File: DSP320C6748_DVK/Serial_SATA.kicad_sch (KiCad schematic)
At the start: 10 parts, among them IC6 CP2102C-A01-GQFN24, J3 USB_Type_C

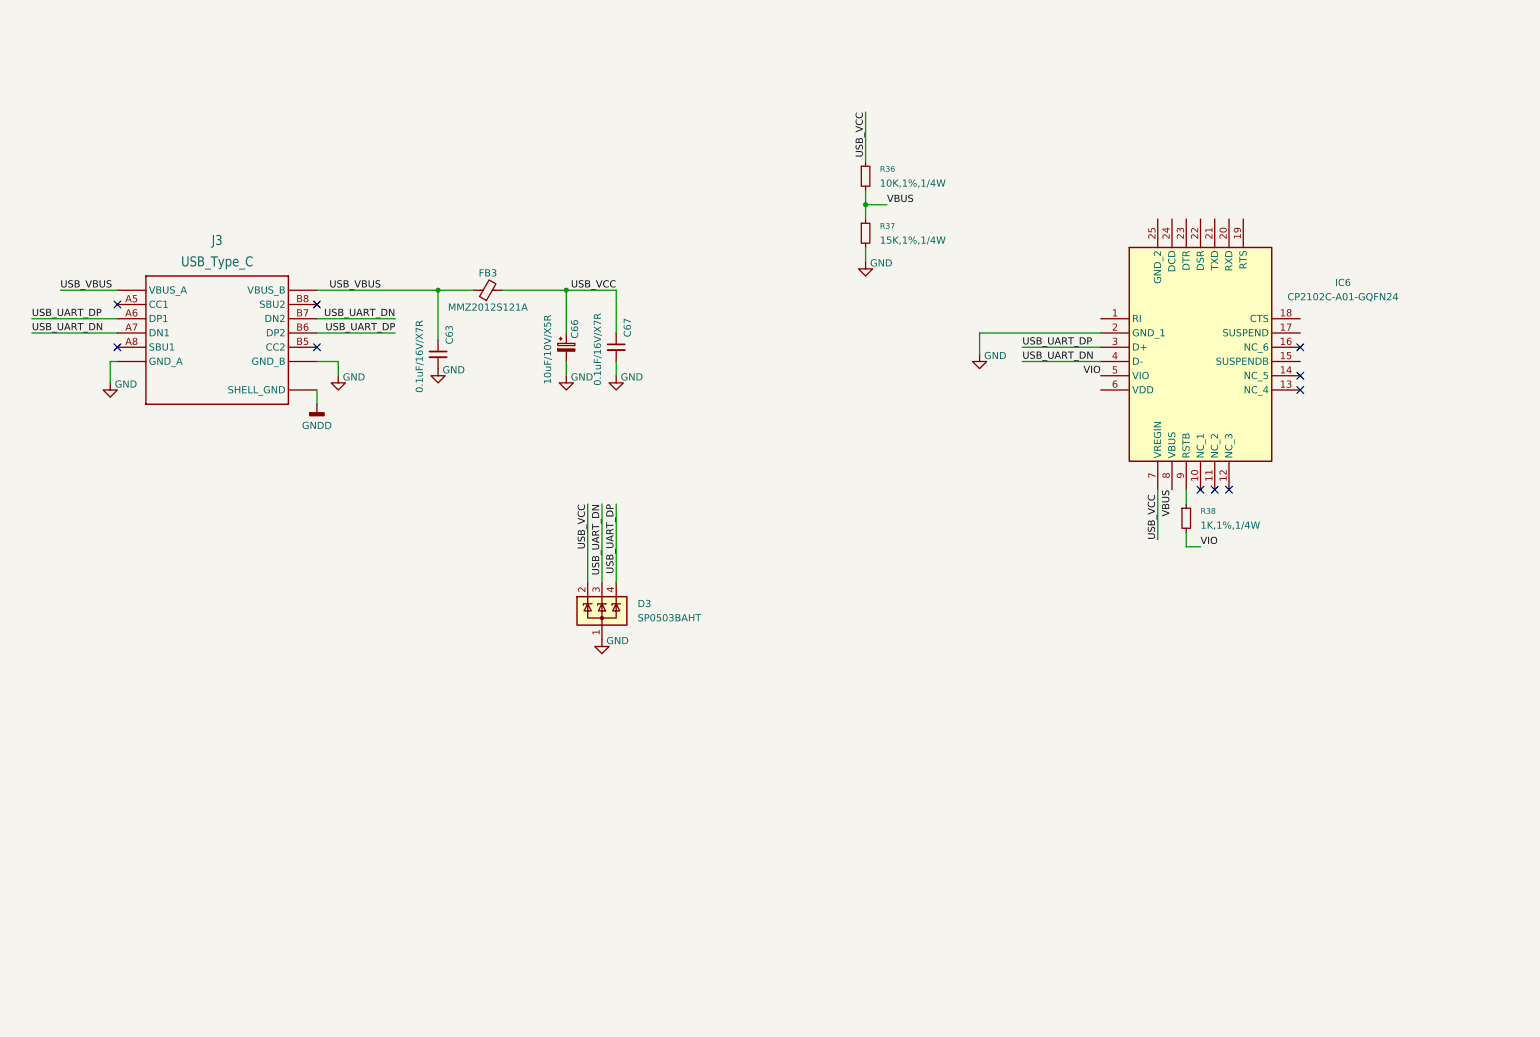
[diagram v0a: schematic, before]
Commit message: Serial Circuit completed, SATA section Added, DSP Reset Section Added
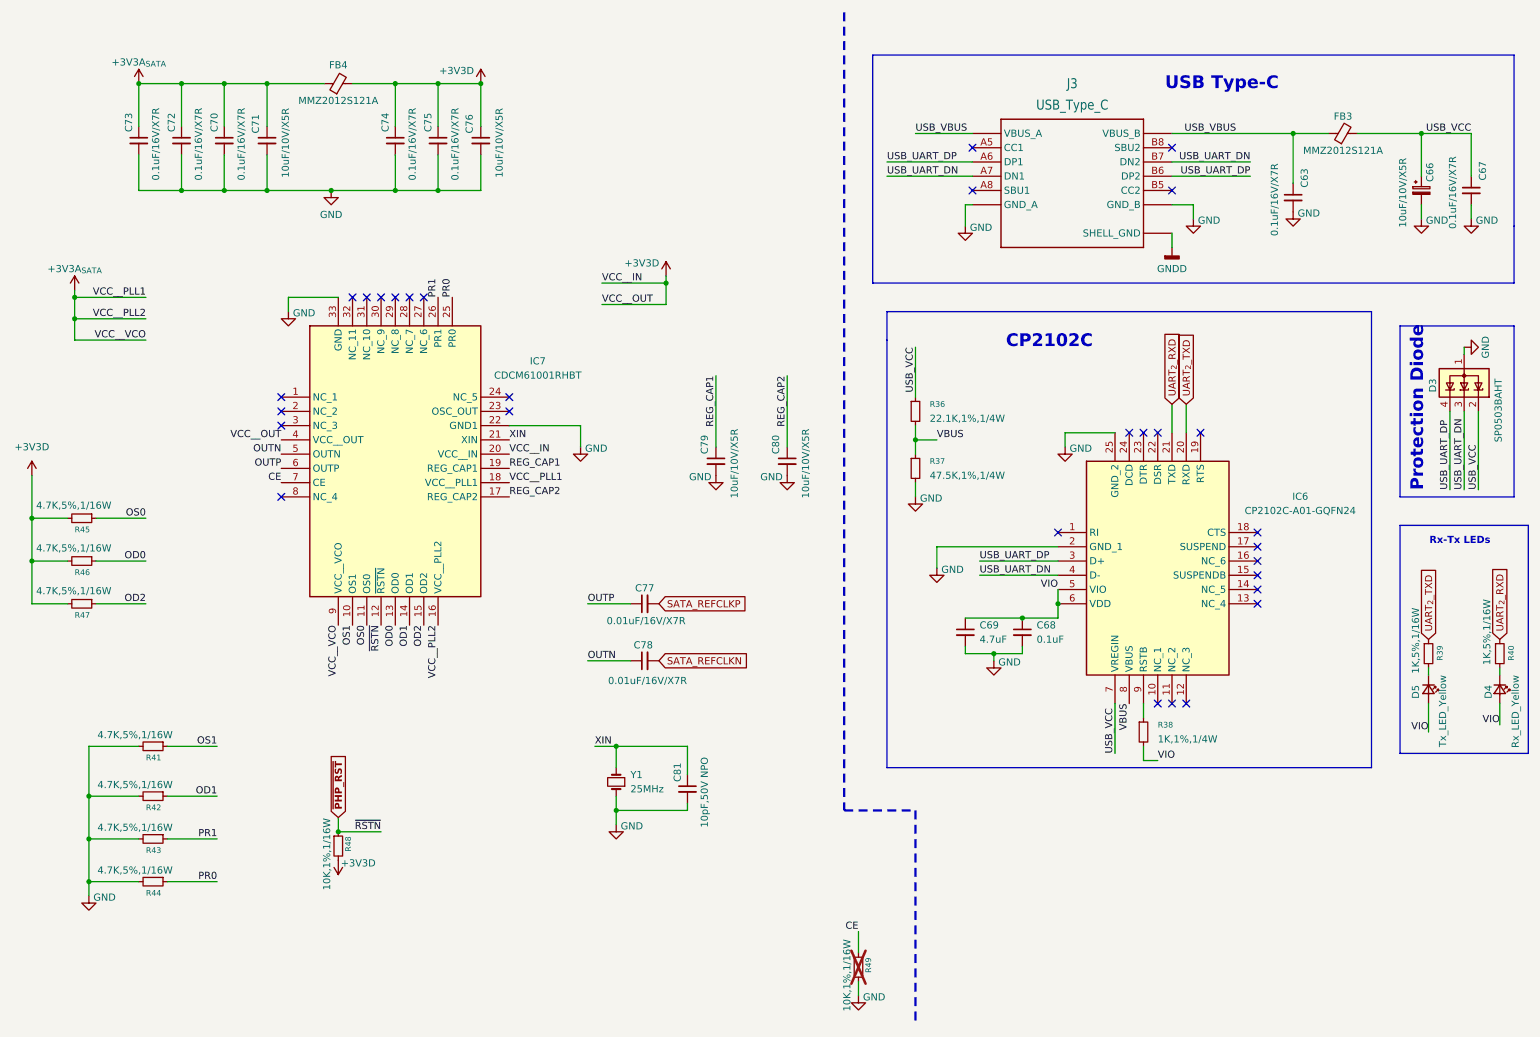
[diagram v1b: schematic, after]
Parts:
- added C68: 0.1uF, symbol Device:C_Small
- added C69: 4.7uF, symbol Device:C_Small
- added C70, C72, C73, C74, C75: 0.1uF/16V/X7R, symbol Device:C_Small
- added C71, C76, C79, C80: 10uF/10V/X5R, symbol Device:C_Small
- added C77, C78: 0.01uF/16V/X7R, symbol Device:C_Small
- added C81: 10pF,50V NPO, symbol Device:C_Small
- added D4: Rx_LED_Yellow, symbol Device:LED_Small
- added D5: Tx_LED_Yellow, symbol Device:LED_Small
- added FB4: MMZ2012S121A, symbol Device:FerriteBead_Small
- added IC7: CDCM61001RHBT, QFN50P500X500X100-33N-D, symbol CDCM61001RHBT:CDCM61001RHBT
- added R39, R40: 1K,5%,1/16W, symbol Device:R_Small
- added R41, R42, R43, R44, R45, R46, R47: 4.7K,5%,1/16W, symbol Device:R_Small
- added R48, R49: 10K,1%,1/16W, symbol Device:R_Small
- added Y1: 25MHz, symbol Device:Crystal_Small
- R36: value 10K,1%,1/4W -> 22.1K,1%,1/4W
- R37: value 15K,1%,1/4W -> 47.5K,1%,1/4W
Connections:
- net GND: now also IC6.25 (GND_2), C68.2, C69.2, C70.2, C71.2, C72.2, C73.2, C74.2, C75.2, C76.2, C79.2, C80.2, C81.2, IC7.22 (GND1), IC7.33 (GND), R41.2, R42.2, R43.2, R44.2, R49.2, Y1.1
- net VIO: now also IC6.6 (VDD), C68.1, C69.1, D4.2 (A), D5.2 (A)
- net UART_{2}_TXD: now reaches IC6.20 (RXD)
- net UART_{2}_TXD: now also R39.1
- net UART_{2}_RXD: now reaches IC6.21 (TXD)
- net UART_{2}_RXD: now also R40.1
- new net: D5.1 (K), R39.2
- new net: D4.1 (K), R40.2
- new net +3V3A_{SATA}: C70.1, C71.1, C72.1, C73.1, FB4.1, IC7.16 (VCC__PLL2), IC7.18 (VCC__PLL1), IC7.9 (VCC__VCO)
- new net +3V3D: C74.1, C75.1, C76.1, FB4.2, IC7.20 (VCC__IN), IC7.4 (VCC__OUT), R45.2, R46.2, R47.2, R48.2
- new net CE: IC7.7 (CE), R49.1
- new net OD0: IC7.13 (OD0), R46.1
- new net OD1: IC7.14 (OD1), R42.1
- new net OD2: IC7.15 (OD2), R47.1
- new net OS0: IC7.11 (OS0), R45.1
- new net OS1: IC7.10 (OS1), R41.1
- new net OUTN: C78.1, IC7.5 (OUTN)
- new net OUTP: C77.1, IC7.6 (OUTP)
- new net PR0: IC7.25 (PR0), R44.1
- new net PR1: IC7.26 (PR1), R43.1
- new net REG_CAP1: C79.1, IC7.19 (REG_CAP1)
- new net REG_CAP2: C80.1, IC7.17 (REG_CAP2)
- new net SATA_REFCLKN: C78.2
- new net SATA_REFCLKP: C77.2
- new net XIN: C81.1, IC7.21 (XIN), Y1.2
- new net ~{PHP_RST}: IC7.12 (~{RSTN}), R48.1
- no-connect marks 10 -> 30
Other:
- note added: "CP2102C"
- note added: "Protection Diode"
- note added: "Rx-Tx LEDs"
- note added: "USB Type-C"
- moved on the sheet: C63, C66, C67, D3, FB3, IC6, J3, R36, R37, R38

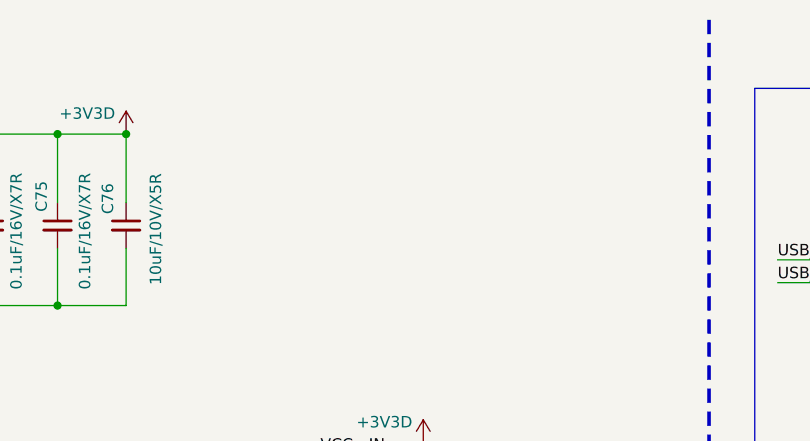
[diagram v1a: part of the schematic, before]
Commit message: Partial VGA-LCD schematic added
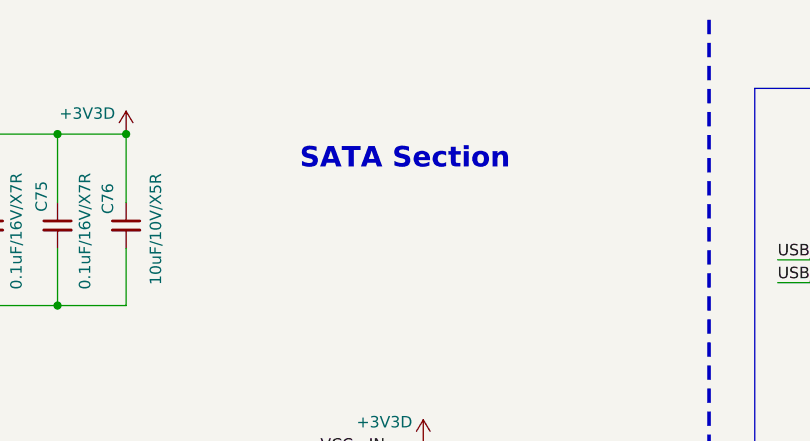
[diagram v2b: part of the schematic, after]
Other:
- note added: "SATA Section"
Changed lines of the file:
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@@
+		)
+	)
+	(text "SATA Section"
+		(exclude_from_sim no)
+		(at 126.238 30.734 0)
+		(effects
+			(font
+				(size 2.27 2.27)
+				(thickness 0.454)
+				(bold yes)
+			)
 		)
 	)

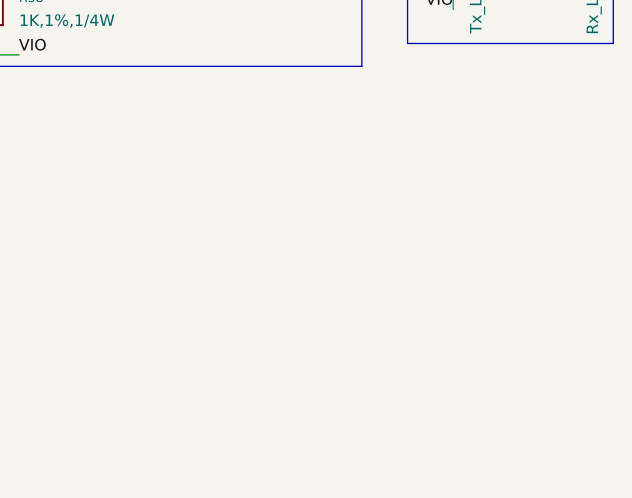
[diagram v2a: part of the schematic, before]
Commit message: DDR_RAM and Video Decoder Schematic Added
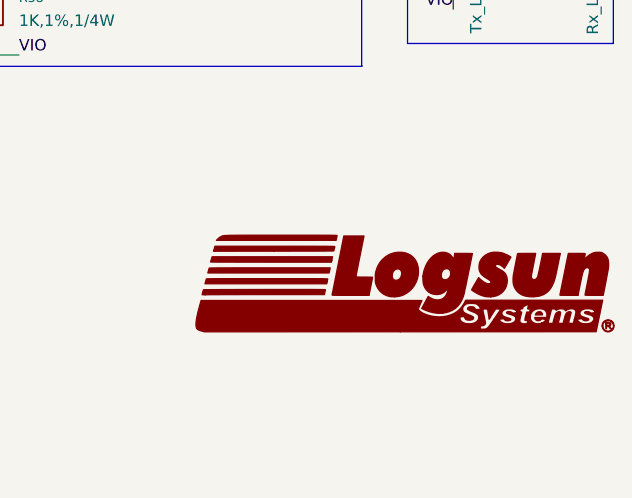
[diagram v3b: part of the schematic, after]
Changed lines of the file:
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@@
+	)
+	(symbol
+		(lib_id "Logsun_Logo:LOGO")
+		(at 259.08 173.99 0)
+		(unit 1)
+		(body_style 1)
+		(exclude_from_sim no)
+		(in_bom yes)
+		(on_board yes)
+		(in_pos_files yes)
+		(dnp no)
+		(fields_autoplaced yes)
+		(property "Reference" "#G7"
+			(at 259.08 168.025 0)
+			(hide yes)
+			(show_name no)
+			(do_not_autoplace no)
+			(effects
+				(font
+					(size 1.27 1.27)
+				)
+			)
+		)
+		(property "Value" "LOGO"
+			(at 259.08 179.955 0)
+			(hide yes)
+			(show_name no)
+			(do_not_autoplace no)
+			(effects
+				(font
+					(size 1.27 1.27)
+				)
+			)
+		)
+		(property "Footprint" ""
+			(at 259.08 173.99 0)
+			(hide yes)
+			(show_name no)
+			(do_not_autoplace no)
+			(effects
+				(font
+					(size 1.27 1.27)
+				)
+			)
+		)
+		(property "Datasheet" ""
+			(at 259.08 173.99 0)
+			(hide yes)
+			(show_name no)
+			(do_not_autoplace no)
+			(effects
+				(font
+					(size 1.27 1.27)
+				)
+			)
+		)
+		(property "Description" ""
+			(at 259.08 173.99 0)
+			(hide yes)
+			(show_name no)
+			(do_not_autoplace no)
+			(effects
+				(font
+					(size 1.27 1.27)
+				)
+			)
+		)
+		(instances
+			(project "DSP320C6748_DVK"
+				(path "/3a70ffc0-9fe7-4a5b-b3c2-23140355df82/1c65a424-dd23-4a5f-aa20-bdb9d16cf58b"
+					(reference "#G7")
+					(unit 1)
+				)
+			)
+		)
 	)
 	(symbol

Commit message: Whole Schematic Reannotation Done
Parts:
- renumbered C73 to C72, C72 to C73, C70 to C74, C71 to C75, C74 to C76, C75 to C77, C76 to C78, C77 to C79, C78 to C80, C79 to C82, C80 to C83, C69 to C84, C68 to C85, C63 to C86, C66 to C87, C67 to C88, D3 to D6, D4 to D7, FB4 to FB3, FB3 to FB4, IC6 to IC10, IC7 to IC9, J3 to J5, R45 to R72, R46 to R73, R47 to R74, R41 to R75, R42 to R76, R43 to R77, R44 to R78, R48 to R79, R49 to R80, R36 to R81, R37 to R82, R38 to R83, R39 to R84, R40 to R85, Y1 to Y3

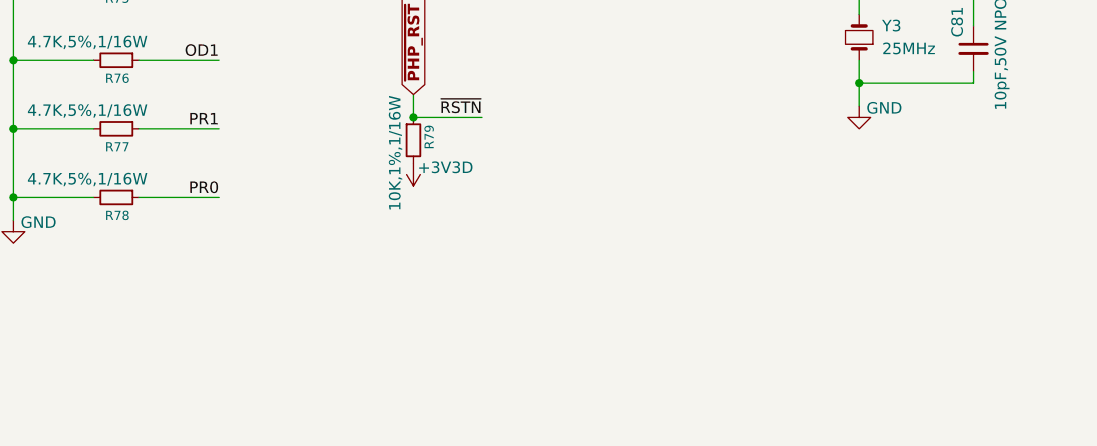
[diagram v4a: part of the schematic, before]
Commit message: SATA Connector Added
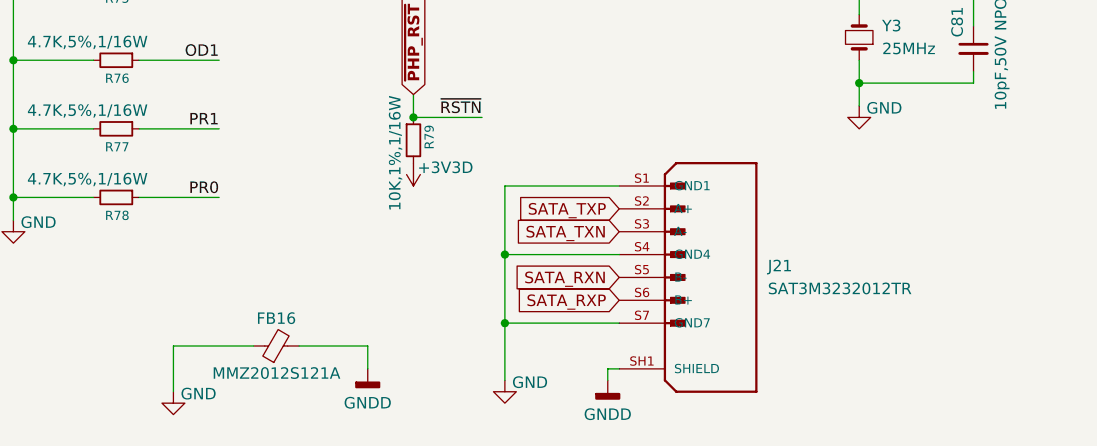
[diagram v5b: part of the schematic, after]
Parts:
- added FB16: MMZ2012S121A, symbol Device:FerriteBead_Small
- added J21: SAT3M3232012TR, SAT3M3232012TR:AMPHENOL_SAT3M3232012TR, symbol SAT3M3232012TR:SAT3M3232012TR
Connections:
- net GND: now also FB16.1, J21.S1 (GND1), J21.S4 (GND4), J21.S7 (GND7)
- net GNDD: now also FB16.2, J21.SH1 (SHIELD), J21.SH2 (SHIELD)
- new net SATA_RXN: J21.S5 (B-)
- new net SATA_RXP: J21.S6 (B+)
- new net SATA_TXN: J21.S3 (A-)
- new net SATA_TXP: J21.S2 (A+)

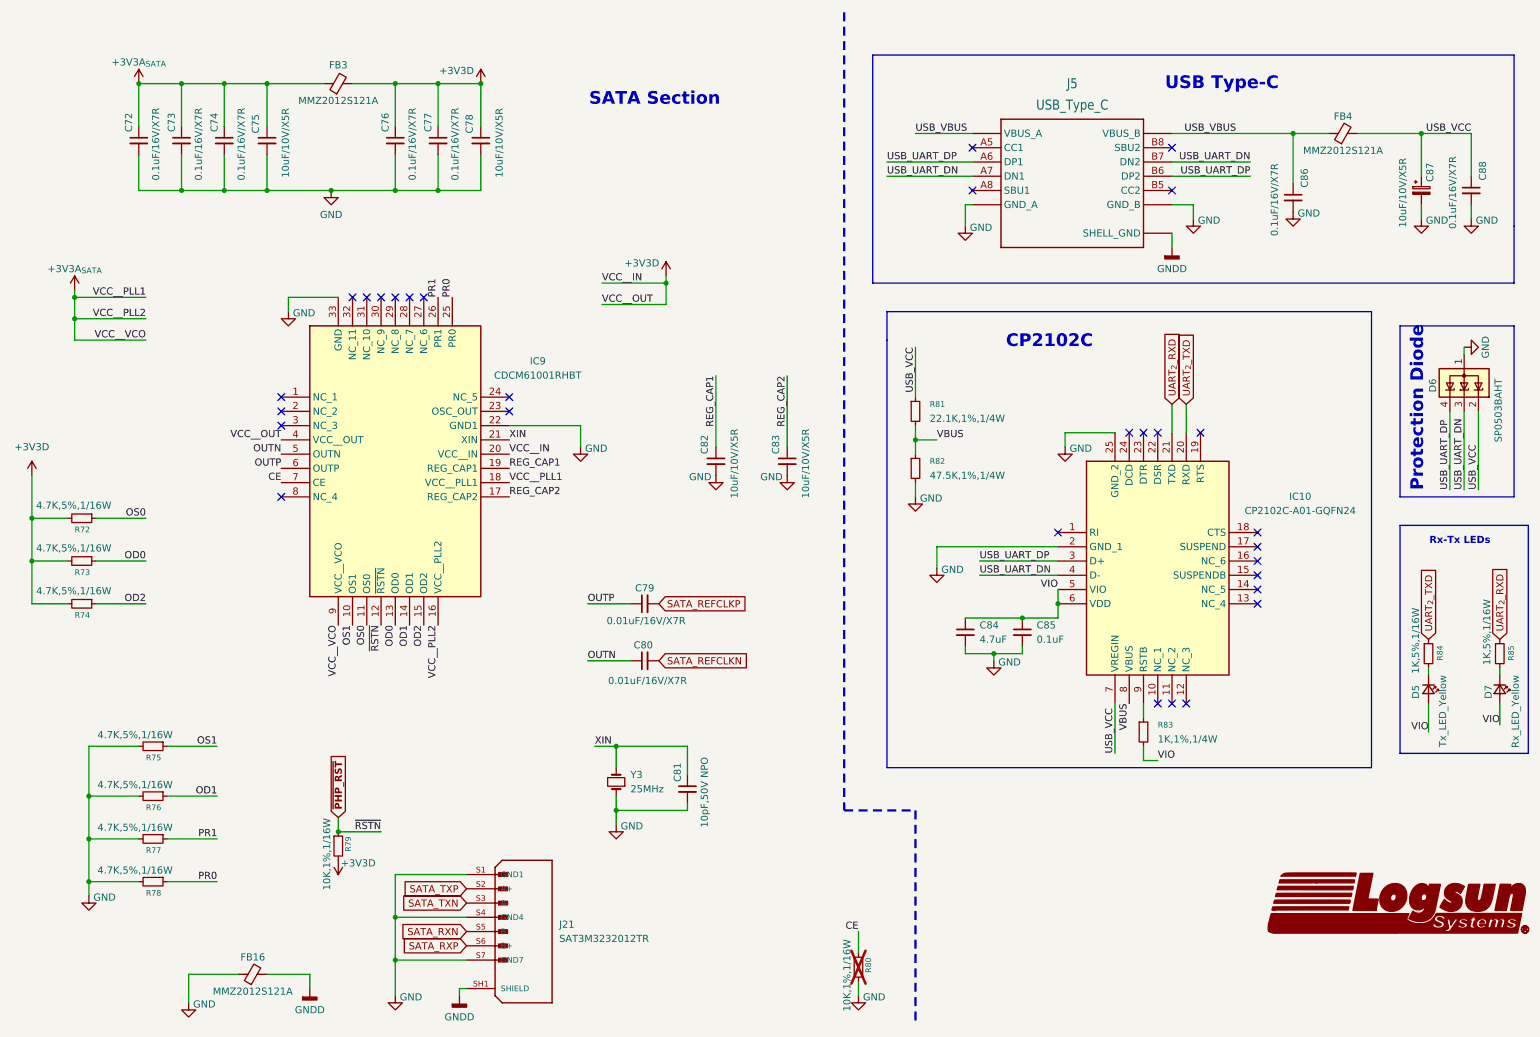
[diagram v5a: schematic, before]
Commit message: DC jack Replaced With Type-C, ADC and RTC section added
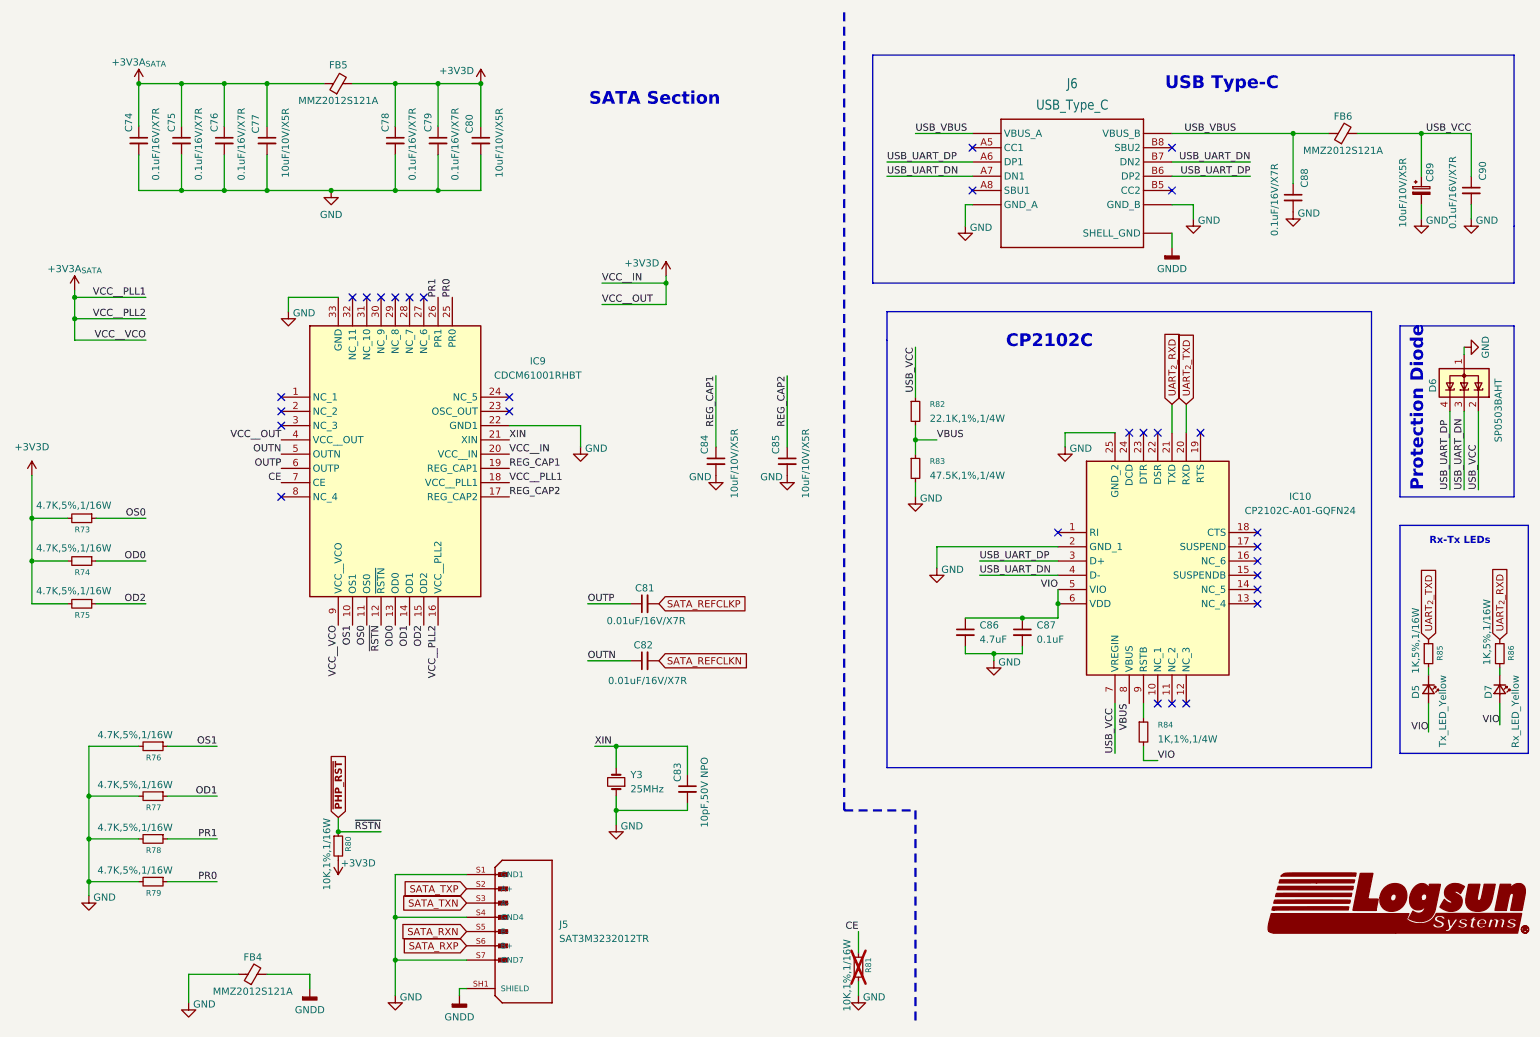
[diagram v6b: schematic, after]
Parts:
- renumbered C72 to C74, C73 to C75, C74 to C76, C75 to C77, C76 to C78, C77 to C79, C78 to C80, C79 to C81, C80 to C82, C81 to C83, C82 to C84, C83 to C85, C84 to C86, C85 to C87, C86 to C88, C87 to C89, C88 to C90, FB16 to FB4, FB3 to FB5, FB4 to FB6, J21 to J5, J5 to J6, R72 to R73, R73 to R74, R74 to R75, R75 to R76, R76 to R77, R77 to R78, R78 to R79, R79 to R80, R80 to R81, R81 to R82, R82 to R83, R83 to R84, R84 to R85, R85 to R86
